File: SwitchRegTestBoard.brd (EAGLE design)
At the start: 44.9 x 33.2 mm, 17 parts

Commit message: Prepare foor etch
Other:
- board text added: "Switcher Test Brd 2013-03-24"
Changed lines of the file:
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@@
 <wire x1="44.938" y1="33.198" x2="0" y2="33.198" width="0" layer="20"/>
 <wire x1="0" y1="33.198" x2="0" y2="0" width="0" layer="20"/>
+<text x="2.286" y="28.448" size="1.016" layer="1">Switcher Test Brd
+2013-03-24</text>
 </plain>
 <attributes>
@@
 <wire x1="6.9057" y1="20.338" x2="8.382" y2="21.608" width="1.016" layer="1"/>
 <wire x1="6.9057" y1="20.0072" x2="6.9057" y2="20.338" width="1.016" layer="1"/>
-<polygon width="0.254" layer="1" spacing="0.4064" pour="hatch" isolate="0.254" rank="3">
-<vertex x="0" y="30.988"/>
+<polygon width="0.254" layer="1" spacing="0.508" pour="hatch" isolate="0.3048" rank="3">
+<vertex x="0" y="33.02"/>
 <vertex x="0" y="-0.254"/>
 <vertex x="44.45" y="-0.254"/>
-<vertex x="44.45" y="30.988"/>
-</polygon>
+<vertex x="44.45" y="33.02"/>
+</polygon>
+<wire x1="34.798" y1="5.08" x2="37.338" y2="5.08" width="0" layer="19" extent="1-1"/>
+<wire x1="42.037" y1="18.796" x2="37.338" y2="5.08" width="0" layer="19" extent="1-1"/>
 </signal>
 <signal name="VR1L">
@@
 <wire x1="21.336" y1="17.526" x2="19.4564" y2="17.399" width="0.3048" layer="1"/>
 <wire x1="21.066" y1="14.351" x2="25.781" y2="15.53" width="0.3048" layer="1"/>
-<polygon width="0.3048" layer="1">
+<polygon width="0.3048" layer="1" isolate="0.254">
 <vertex x="19.431" y="16.891"/>
-<vertex x="20.955" y="16.891"/>
+<vertex x="20.701" y="16.637"/>
 <vertex x="21.209" y="13.843"/>
-<vertex x="25.781" y="13.843"/>
-<vertex x="26.035" y="17.653"/>
-<vertex x="19.431" y="17.653"/>
+<vertex x="29.337" y="13.589"/>
+<vertex x="28.575" y="18.415"/>
+<vertex x="19.431" y="18.161"/>
 </polygon>
 </signal>
@@
 <contactref element="JP1" pad="4"/>
 <contactref element="C4" pad="+"/>
-<polygon width="0.3048" layer="1">
+<polygon width="0.3048" layer="1" isolate="0.254">
 <vertex x="1.524" y="14.986"/>
 <vertex x="6.096" y="14.986"/>
@@
 <vertex x="12.7" y="18.542"/>
 <vertex x="11.557" y="18.034"/>
-<vertex x="11.557" y="16.002"/>
-<vertex x="8.89" y="15.875"/>
+<vertex x="11.811" y="15.24"/>
+<vertex x="9.398" y="15.113"/>
 <vertex x="7.239" y="11.43"/>
 <vertex x="1.524" y="11.43"/>
@@
 <polygon width="0.3048" layer="1">
 <vertex x="15.875" y="23.749"/>
-<vertex x="23.368" y="25.019"/>
-<vertex x="25.273" y="24.765"/>
+<vertex x="23.114" y="25.527"/>
+<vertex x="27.051" y="25.273"/>
 <vertex x="28.956" y="23.368"/>
 <vertex x="28.448" y="18.415"/>
@@
 <vertex x="15.875" y="21.336"/>
 </polygon>
-<polygon width="0.3048" layer="1">
-<vertex x="28.448" y="18.288"/>
+<polygon width="0.3048" layer="1" isolate="0.254">
+<vertex x="29.21" y="19.05"/>
 <vertex x="30.734" y="17.526"/>
 <vertex x="33.274" y="13.462"/>
@@
 </board>
 </drawing>
+<compatibility>
+<note version="6.3" minversion="6.2.2" severity="warning">
+Since Version 6.2.2 text objects can contain more than one line,
+which will not be processed correctly with this version.
+</note>
+</compatibility>
 </eagle>

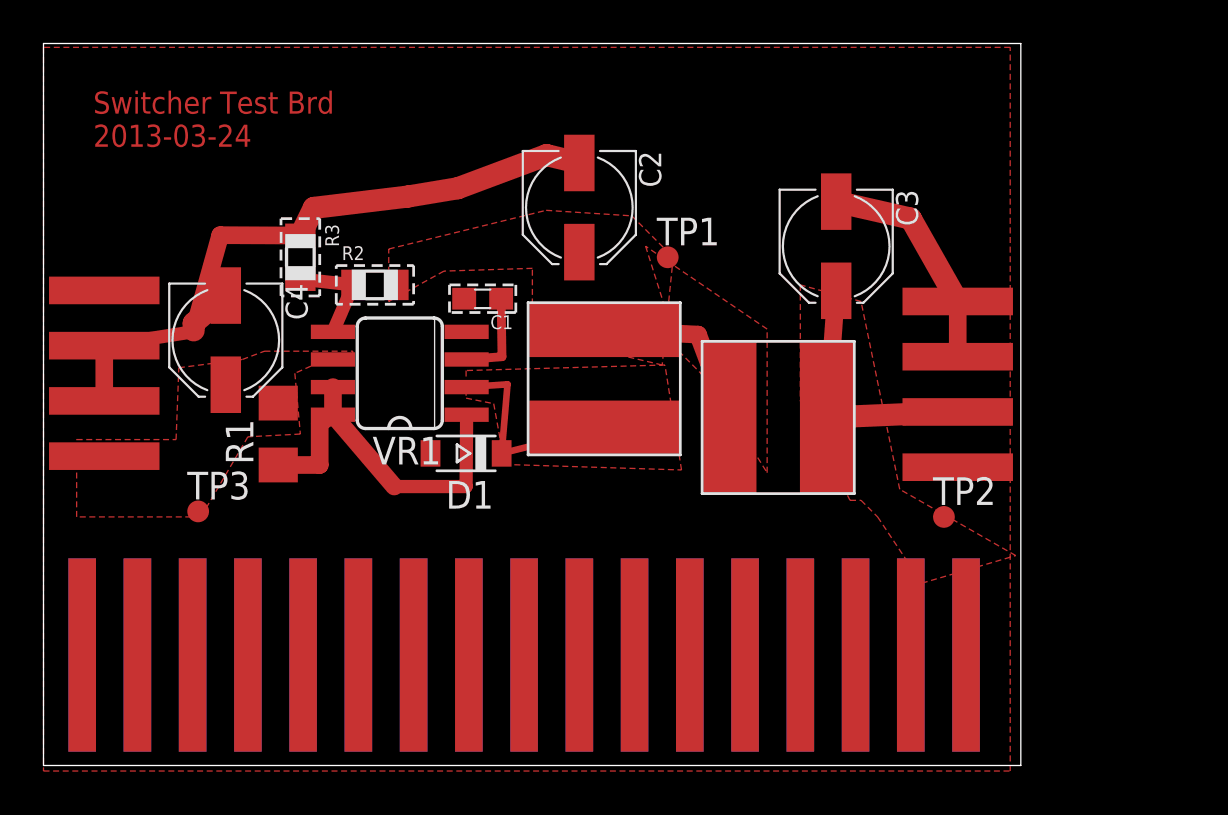
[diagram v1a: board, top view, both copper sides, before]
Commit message: star ground around switcher.  Additional resistor pad for low side of divider for tweaking resistance
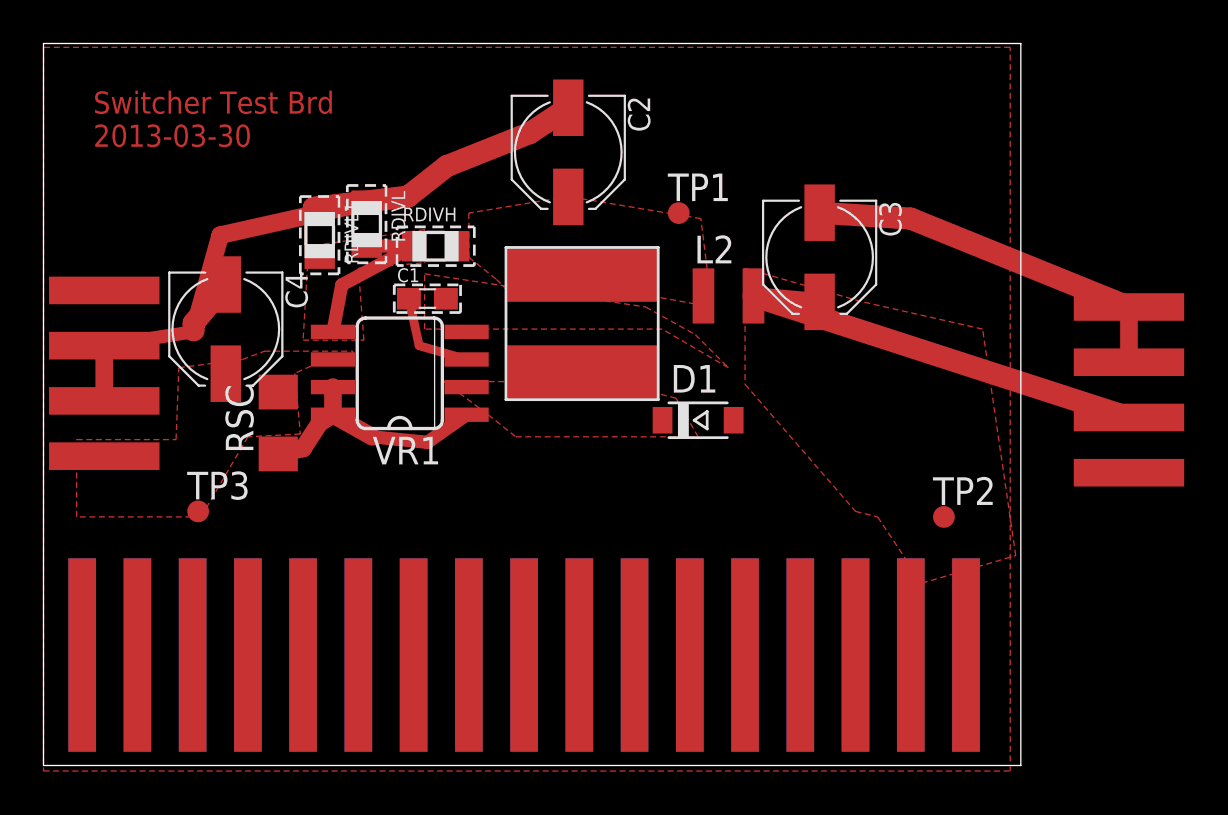
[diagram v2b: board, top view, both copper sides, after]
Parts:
- removed R1: 1.5, LL:R1206
- removed R2: 16k, LL:R0805
- removed R3: 10k, LL:R0805
- added RDIVH: 16k, LL:R0805
- added RDIVL, RDIVL1: 10k, LL:R0805
- added RSC: 1.5, LL:R1206
- L2: device LL:L0707MM -> inductor-neosid:SM-NE29
- moved D1 10.8 mm to (30.1, 15.9), turned to 0 degrees
- moved JP2 7.88 mm to (49.9, 17.3)
- moved L2 6.04 mm to (31.5, 21.6), turned to 0 degrees
- moved L1 2.74 mm to (24.8, 20.3)
- moved C2 2.59 mm to (24.1, 28.2)
- moved C1 2.54 mm to (17.7, 21.5), turned to 0 degrees
- moved TP1 2.09 mm to (29.2, 25.4)
- moved C3 0.92 mm to (35.7, 23.4)
- moved C4 0.51 mm to (8.38, 20.1)
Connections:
- removed net N$6: R2.1, R3.2, VR1.5
- new net DIVIDERCENTER: RDIVH.1, RDIVL.2, RDIVL1.2, VR1.5
- net GND: now also RDIVL.1, RDIVL1.1; no longer R3.1
- net N$2: now also RSC.1; no longer R1.1
- net VIN: now also RSC.2; no longer R1.2
- net VROUT33: now also RDIVH.2; no longer R2.2
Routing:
- net GND: track 41.7 -> 53.7 mm
- net VR1L: track 9.93 -> 0.00 mm
- net VRFOUT33: track 11.8 -> 21.2 mm
- net VROUT33: track 8.39 -> 0.00 mm
- net DIVIDERCENTER: track 0.00 -> 8.14 mm
- net N$2: track 16.8 -> 11.4 mm
- net N$6: track 4.79 -> 0.00 mm
- added copper zone on layer 1, net DIVIDERCENTER
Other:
- board text added: "Switcher Test Brd 2013-03-30"
- board text removed: "Switcher Test Brd 2013-03-24"

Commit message: polygon tuning
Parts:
- moved JP2 10.2 mm to (41.0, 22.4)
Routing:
- net VRFOUT33: track 21.2 -> 11.4 mm
- net GND: track 53.7 -> 44.4 mm
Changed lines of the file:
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@@
 <element name="C3" library="LL" package="PANASONIC_C" value="100uf" x="35.687" y="23.368" rot="R270"/>
 <element name="JP1" library="LL" package="1X04-SMD-LONG" value="" x="2.794" y="18.034" rot="R270"/>
-<element name="JP2" library="LL" package="1X04-SMD-LONG" value="" x="49.911" y="17.272" rot="R90"/>
+<element name="JP2" library="LL" package="1X04-SMD-LONG" value="" x="41.021" y="22.352" rot="R90"/>
 <element name="D1" library="dp_devices" package="SOD-123" value="SHOTTKY" x="30.099" y="15.875"/>
 <element name="C4" library="LL" package="PANASONIC_C" value="100uf" x="8.382" y="20.066" rot="R270"/>
@@
 <wire x1="6.9057" y1="20.0072" x2="8.128" y2="24.384" width="0.8128" layer="1"/>
 <wire x1="8.128" y1="24.384" x2="14.859" y2="25.892" width="0.8128" layer="1"/>
-<wire x1="49.911" y1="21.082" x2="39.878" y2="25.146" width="1.016" layer="1"/>
+<wire x1="41.021" y1="26.162" x2="39.878" y2="25.146" width="1.016" layer="1"/>
 <wire x1="39.878" y1="25.146" x2="35.687" y2="25.418" width="1.016" layer="1"/>
-<wire x1="49.911" y1="18.542" x2="49.911" y2="21.082" width="0.8128" layer="1"/>
+<wire x1="41.021" y1="23.622" x2="41.021" y2="26.162" width="0.8128" layer="1"/>
 <wire x1="14.859" y1="25.892" x2="12.43" y2="25.638" width="1.016" layer="1"/>
 <wire x1="12.43" y1="25.638" x2="16.764" y2="26.162" width="1.016" layer="1"/>
@@
 <polygon width="0.254" layer="1" isolate="0.254">
 <vertex x="17.526" y="22.606"/>
-<vertex x="27.686" y="21.082"/>
+<vertex x="19.812" y="22.606"/>
+<vertex x="21.082" y="21.082"/>
+<vertex x="28.194" y="21.082"/>
 <vertex x="29.972" y="19.812"/>
 <vertex x="31.496" y="18.288"/>
@@
 <polygon width="0.254" layer="1" isolate="0.254">
 <vertex x="12.192" y="23.876"/>
-<vertex x="11.938" y="19.558"/>
+<vertex x="11.684" y="19.558"/>
 <vertex x="14.732" y="19.558"/>
 <vertex x="14.478" y="22.86"/>
@@
 <contactref element="U$1" pad="2_DCD"/>
 <wire x1="32.646" y1="21.59" x2="35.687" y2="21.318" width="0.8128" layer="1"/>
-<wire x1="32.646" y1="21.59" x2="49.911" y2="16.002" width="1.016" layer="1"/>
+<wire x1="32.646" y1="21.59" x2="41.021" y2="21.082" width="1.016" layer="1"/>
 <polygon width="0.3048" layer="1">
 <vertex x="40.386" y="8.382"/>
@@
 </polygon>
 <contactref element="TP1" pad="TP"/>
-<wire x1="30.346" y1="21.59" x2="49.911" y2="13.462" width="0" layer="19" extent="1-1"/>
+<wire x1="30.346" y1="21.59" x2="41.021" y2="18.542" width="0" layer="19" extent="1-1"/>
 </signal>
 <signal name="1_GND">
